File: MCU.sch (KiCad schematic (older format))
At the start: 42 parts, among them P801 JTAG, P802 A7, P803 M4, U801 MCIMX7D7DVM10SC, Y801 32kHz, Y802 24MHz

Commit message: This branch moves from i.mx7 to STM32F4 CPU to be finished for Hackaday Prize 2017
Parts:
- removed C805, C807, C810: 220n, Capacitors_SMD:C_0402, symbol C
- removed C806: 22u, Capacitors_SMD:C_0603, symbol C
- removed C808, C814, C815, C818: 2u2, Capacitors_SMD:C_0603, symbol C
- removed C809: 100n, Capacitors_SMD:C_0402, symbol C
- removed C811, C812, C813, C816, C817: 470n, Capacitors_SMD:C_0402, symbol C
- removed D801: D_Schottky, Diodes_SMD:DD-PAK_TO263_SingleDiode, symbol D_Schottky
- removed L801: 100R, Choke_SMD:Choke_SMD_1206_Standard, symbol L_Small
- removed P802: A7, Pin_Headers:Pin_Header_Straight_1x02, symbol CONN_01X02
- removed P803: M4, Pin_Headers:Pin_Header_Straight_1x02, symbol CONN_01X02
- removed R802, R810, R814, R815: 0, Resistors_SMD:R_0402, symbol R
- removed R803: 100k, Resistors_SMD:R_0402, symbol R
- removed R808: 10k, Resistors_SMD:R_0402, symbol R
- removed R809: 4k7, Resistors_SMD:R_0402, symbol R
- removed R811, R812: 1k, Resistors_SMD:R_0402, symbol R
- removed R813: 47k, Resistors_SMD:R_0402, symbol R
- removed U801: MCIMX7D7DVM10SC, NokiaRetroFit:BGA_541_075_19x19, symbol MCIMX7D7DVM10SC
- added C? (x8): 100n, Capacitors_SMD:C_0402, symbol C
- added C? (x2): 2u2, Capacitors_SMD:C_0402, symbol C
- added C?: 1u, Capacitors_SMD:C_0402, symbol C
- added J?: TEST_2P, symbol TEST_2P
- added R? (x2): 10k, symbol R
- added U?: STM32F756VGTx, LQFP100, symbol STM32F756VGTx
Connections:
- net labels added: ADC1, ADC2, ADC3, ADC_IN1, ADC_IN2, ADC_IN3, ETC_ALARM, I2C3_SCL, I2C3_SDA, I2C4_SCL, I2C4_SDA, JTAG_RST, JTAG_TCK, JTAG_TDI, JTAG_TDO, JTAG_TMS, LCD_RS, QSPI_BK2_IO0, QSPI_BK2_IO1, QSPI_BK2_IO2, QSPI_BK2_IO3, QSPI_BK2_NCS, QSPI_CLK, QSPI_IO0, QSPI_IO1, QSPI_IO2, QSPI_IO3, QSPI_NCS, RTC_OUT_ALARM, RTC_TS, SAI1_FS, SAI1_FS_A, SAI1_SCK, SAI1_SD, SAI1_SD_A, SAI_MCLK, SAI_MCLK_A, SDMMC1_CK, SDMMC1_CMD, SDMMC1_D0, SD_CK, SD_CMD, SD_D0, SYS_JRST, SYS_JTCK-SWCLK, SYS_JTDI, SYS_JTDO-SWO, SYS_JTMS-SWDIO, SYS_WKUP, TIM10_PWM, UART8_CTS, UART8_RTS, UART8_RX, UART8_TX, USART1_RX, USART1_TX, USART2_RX, USART2_TX, USART3_RX, USART3_TX, USART6_RX, USART6_TX, USB_DM, USB_DP, USB_ID, USB_OTG_HS_DM, USB_OTG_HS_DP, USB_OTG_HS_ID, USB_OTG_HS_VBUS, USB_VBUS, VBAT, nRST
- net labels removed: AT_UART0, AT_UART1, AT_UART2, AT_UART3, AT_UART[0..3], AT_UART_CTS, AT_UART_RTS, AT_UART_RX, AT_UART_TX, BT0, BT1, BT2, BT3, BT[0..7], BT_EN, BT_UART_CTS, BT_UART_RTS, BT_UART_RX, BT_UART_TX, D+, D-, GPIO2_D10, GPIO2_D11, GPIO2_D20, GPIO2_D21, GPIO2_D22, GPIO2_D23, GPIO2_D8, GPIO2_D9, GPS_TX, HST_DL0, HST_DL1, HST_DL[0..1], LCD_CLK, LCD_DATA00, LCD_DATA01, LCD_DATA02, LCD_DATA03, LCD_DATA04, LCD_DATA05, LCD_DATA06, LCD_DATA07, LCD_DATA08, LCD_DATA09, LCD_DATA10, LCD_DATA11, LCD_DATA12, LCD_DATA13, LCD_DATA14, LCD_DATA15, LCD_DATA16, LCD_DATA17, LCD_DATA18, LCD_DATA19, LCD_DATA20, LCD_DATA21, LCD_DATA22, LCD_DATA23, LCD_DATA[0..23], LCD_ENABLE, LCD_HSYNC, LCD_VSYNC, LED_PWM, NVCC_1V8, NVCC_3V3, PMIC_SD_VSEL, PWM1_OUT, PWM2_OUT, PWM3_OUT, PWM4_OUT, RADIO_ON, RUMBLE_EN, RUMBLE_PWM, SAI1[0..6], SAI2[0..3], SD2_BUS[0..8], SW2OUT, UART5_RX, UART7_CTS, UART7_RTS, UART7_RX, UART7_TX, USB_OTG_ID, VBAT_ref, VDC_ref, VDDA, VLDO4_2V8, VSNVS, V_USB_BUS_ref, ~ON, ~POR
- wire segments 223 -> 136
- no-connect marks 16 -> 1
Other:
- note removed: "10"
- note removed: "11"
- note removed: "12"
- note removed: "13"
- note removed: "1GB DDR3 RAM"
- note removed: "uSD-Card Slot\n8GB eMMC"
- moved on the sheet: C801, C802, C803, C804, P801, R801, R804, R805, R806, R807, TP801, Y801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

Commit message: Modification for STM32 adaption
For the Hackaday Prize 2017 I decided to switch to STM32 as CPU

*Power system was modified to just contain the charge IC,
*Boost converter for high voltage peripherals
*Buck converter for 3V3 for CPU and switchable NVCC_3V3
   for peripherie

CPU signals are routed and pinmux is done in firmware folder.

SD-Card has 4bit Interface

WiFi module ESP8266 is connected via UART

Wolfson Ausio codec is connected via SAI

Two digital microphones for noise canceling

Rumble Motor driver

LCD is connected via it's own I2C interface
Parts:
- C801, C802, C803, C804: footprint Capacitors_SMD:C_0402 -> Capacitors_SMD:C_0402_NoSilk
- C805, C806, C807, C808, C809, C810, C811, C812, C813, C814, C815: renamed from C?; footprint Capacitors_SMD:C_0402 -> Capacitors_SMD:C_0402_NoSilk
- J801: renamed from J?; footprint (none) -> Wire_Pads:SolderWirePad_2x_1mmDrill
- R801, R804, R805, R806, R807: footprint Resistors_SMD:R_0402 -> Resistors_SMD:R_0402_NoSilk
- R802, R803: renamed from R?; footprint (none) -> Resistors_SMD:R_0402_NoSilk
- gave numbers to parts that had none: 1
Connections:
- net I2C3_SCL: no longer U801.67 (I2C3_SCL/LTDC_R6/RCC_MCO_1/TIM1_CH1/TIM8_BKIN2/USART1_CK/USB_OTG_FS_SOF/PA8)
- net I2C3_SDA: no longer U801.66 (DAC_EXTI9/DCMI_D3/I2C3_SDA/I2S_CKIN/QUADSPI_BK1_IO0/RCC_MCO_2/SDMMC1_D1/TIM3_CH4/TIM8_CH4/UART5_CTS/PC9)
- net IMU_DRDY_M: now also U801.81 (PD0/CAN1_RX/FMC_D2/FMC_DA2); no longer U801.96 (CAN1_TX/DAC_EXTI9/DCMI_D7/I2C1_SDA/I2S2_WS/LTDC_B7/SDMMC1_D5/SPI2_NSS/TIM11_CH1/TIM4_CH4/PB9)
- net RADIO_ACTIVE: no longer U801.34 (ADC1_IN8/ADC2_IN8/ETH_RXD2/LTDC_R3/TIM1_CH2N/TIM3_CH3/TIM8_CH2N/UART4_CTS/USB_OTG_HS_ULPI_D1/PB0)
- net NVCC_3V3: now reaches C809.1, C810.1, C811.1, C812.1, C813.1, C814.1, C815.1, R803.2, U801.100 (VDD), U801.11 (VDD), U801.21 (VDDA), U801.27 (VDD), U801.50 (VDD), U801.75 (VDD)
- net WIFI_BOOT0: now reaches U801.15 (ADC1_IN10/ADC2_IN10/ADC3_IN10/FMC_SDNWE/LTDC_R5/SAI2_FS_B/USB_OTG_HS_ULPI_STP/PC0)
- net RADIO_ON: now reaches U801.17 (ADC1_IN12/ADC2_IN12/ADC3_IN12/ETH_TXD2/FMC_SDNE0/SPI2_MISO/USB_OTG_HS_ULPI_DIR/PC2)
- net SAI1_SDB: now reaches U801.2 (PE3/FMC_A19/SAI1_SD_B/SYS_TRACED0)
- net U3V3_PG: now reaches U801.32 (ADC1_IN14/ADC2_IN14/ETH_RXD0/FMC_SDNE0/I2S1_MCK/SPDIFRX_IN2/PC4)
- net WIFI_RESET: now reaches U801.70 (ADC1_EXTI11/ADC2_EXTI11/ADC3_EXTI11/CAN1_RX/LTDC_R4/TIM1_CH4/USART1_CTS/USB_OTG_FS_DM/PA11)
- net WIFI_CHPD: now reaches U801.71 (CAN1_TX/LTDC_R5/SAI2_FS_B/TIM1_ETR/USART1_RTS/USB_OTG_FS_DP/PA12)
- net SD_D2: now reaches U801.78 (DCMI_D8/I2S3_CK/LTDC_R2/QUADSPI_BK1_IO1/SDMMC1_D2/SPI3_SCK/UART4_TX/USART3_TX/PC10)
- net RUMBLE_EN: now reaches U801.82 (PD1/CAN1_TX/FMC_D3/FMC_DA3)
- net QSPI_CLK: no longer names the net of U801.36 (I2S3_SD/QUADSPI_CLK/SAI1_SD_A/SPI3_MOSI/PB2)
- net QSPI_CLK: no longer U801.37 (PE7/FMC_D4/FMC_DA4/QUADSPI_BK2_IO0/TIM1_ETR/UART7_RX)
- net QSPI_IO0 renamed PE8
- net QSPI_IO1 renamed PE9
- net QSPI_IO2 renamed PE10
- net QSPI_IO3 renamed NVCC_3V3_EN
- net QSPI_NCS renamed SD_D3
- net SAI1_SCK renamed SAI1_SCKA
- net SAI1_SD renamed SAI1_SDA
- new net AUDIO_INT: U801.34 (ADC1_IN8/ADC2_IN8/ETH_RXD2/LTDC_R3/TIM1_CH2N/TIM3_CH3/TIM8_CH2N/UART4_CTS/USB_OTG_HS_ULPI_D1/PB0)
- new net PE7: U801.37 (PE7/FMC_D4/FMC_DA4/QUADSPI_BK2_IO0/TIM1_ETR/UART7_RX)
- new net SD_D1: U801.66 (DAC_EXTI9/DCMI_D3/I2C3_SDA/I2S_CKIN/QUADSPI_BK1_IO0/RCC_MCO_2/SDMMC1_D1/TIM3_CH4/TIM8_CH4/UART5_CTS/PC9)
- new net TIM11_RUMBLE_PWM: U801.96 (CAN1_TX/DAC_EXTI9/DCMI_D7/I2C1_SDA/I2S2_WS/LTDC_B7/SDMMC1_D5/SPI2_NSS/TIM11_CH1/TIM4_CH4/PB9)

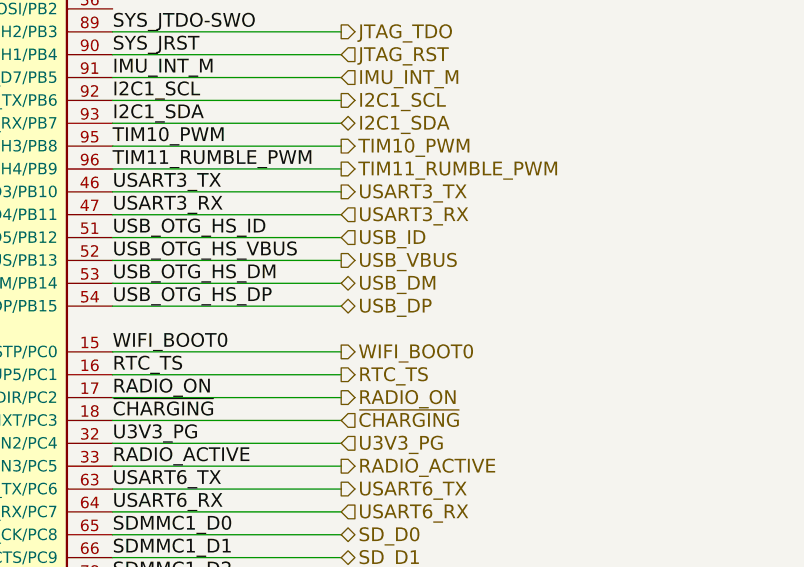
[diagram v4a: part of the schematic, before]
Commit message: Placed a lot of components and routed the audio codec
The BGA of tha audio chipset is to small for regualr technology.
We do not use all of the pins of the chip so we ignore the other
pads and escape throug the balls of the other pad.
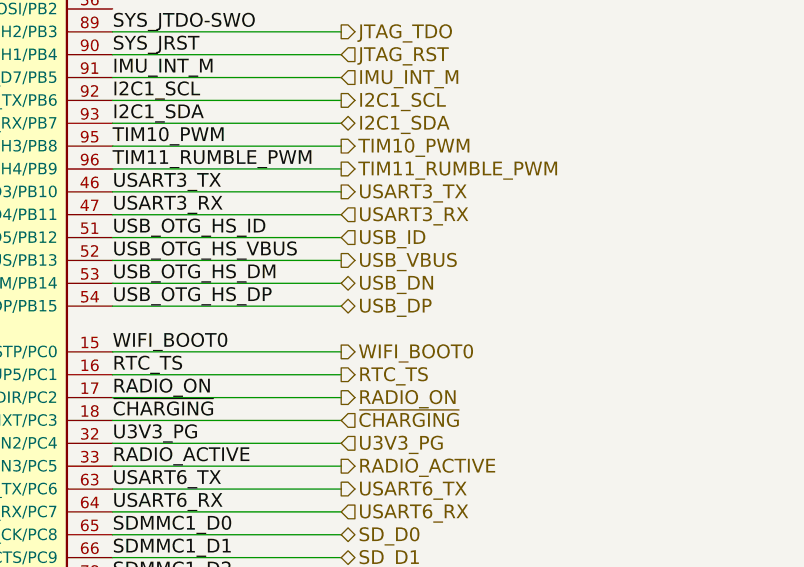
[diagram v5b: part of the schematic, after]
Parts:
- U801: footprint LQFP100 -> Housings_QFP:TQFP-100-1EP_14x14mm_Pitch0.5mm
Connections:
- net USB_DM renamed USB_DN
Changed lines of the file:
@@
 LIBS:contrib
 LIBS:valves
-LIBS:tps62742
-LIBS:WM8994ECS
+LIBS:stm32
 LIBS:3210retro-cache
 EELAYER 26 0
@@
 F 0 "U801" H 12850 8350 50  0000 C CNN
 F 1 "STM32F756VGTx" H 12650 2750 50  0000 C CNN
-F 2 "LQFP100" H 12950 8275 50  0001 R TNN
+F 2 "Housings_QFP:TQFP-100-1EP_14x14mm_Pitch0.5mm" H 12950 8275 50  0001 R TNN
 F 3 "" H 8050 5500 50  0001 C CNN
 	1    8050 5500
@@
 USB_VBUS
 Text HLabel 14150 6100 2    60   BiDi ~ 0
-USB_DM
+USB_DN
 Text HLabel 14150 6200 2    60   BiDi ~ 0
 USB_DP

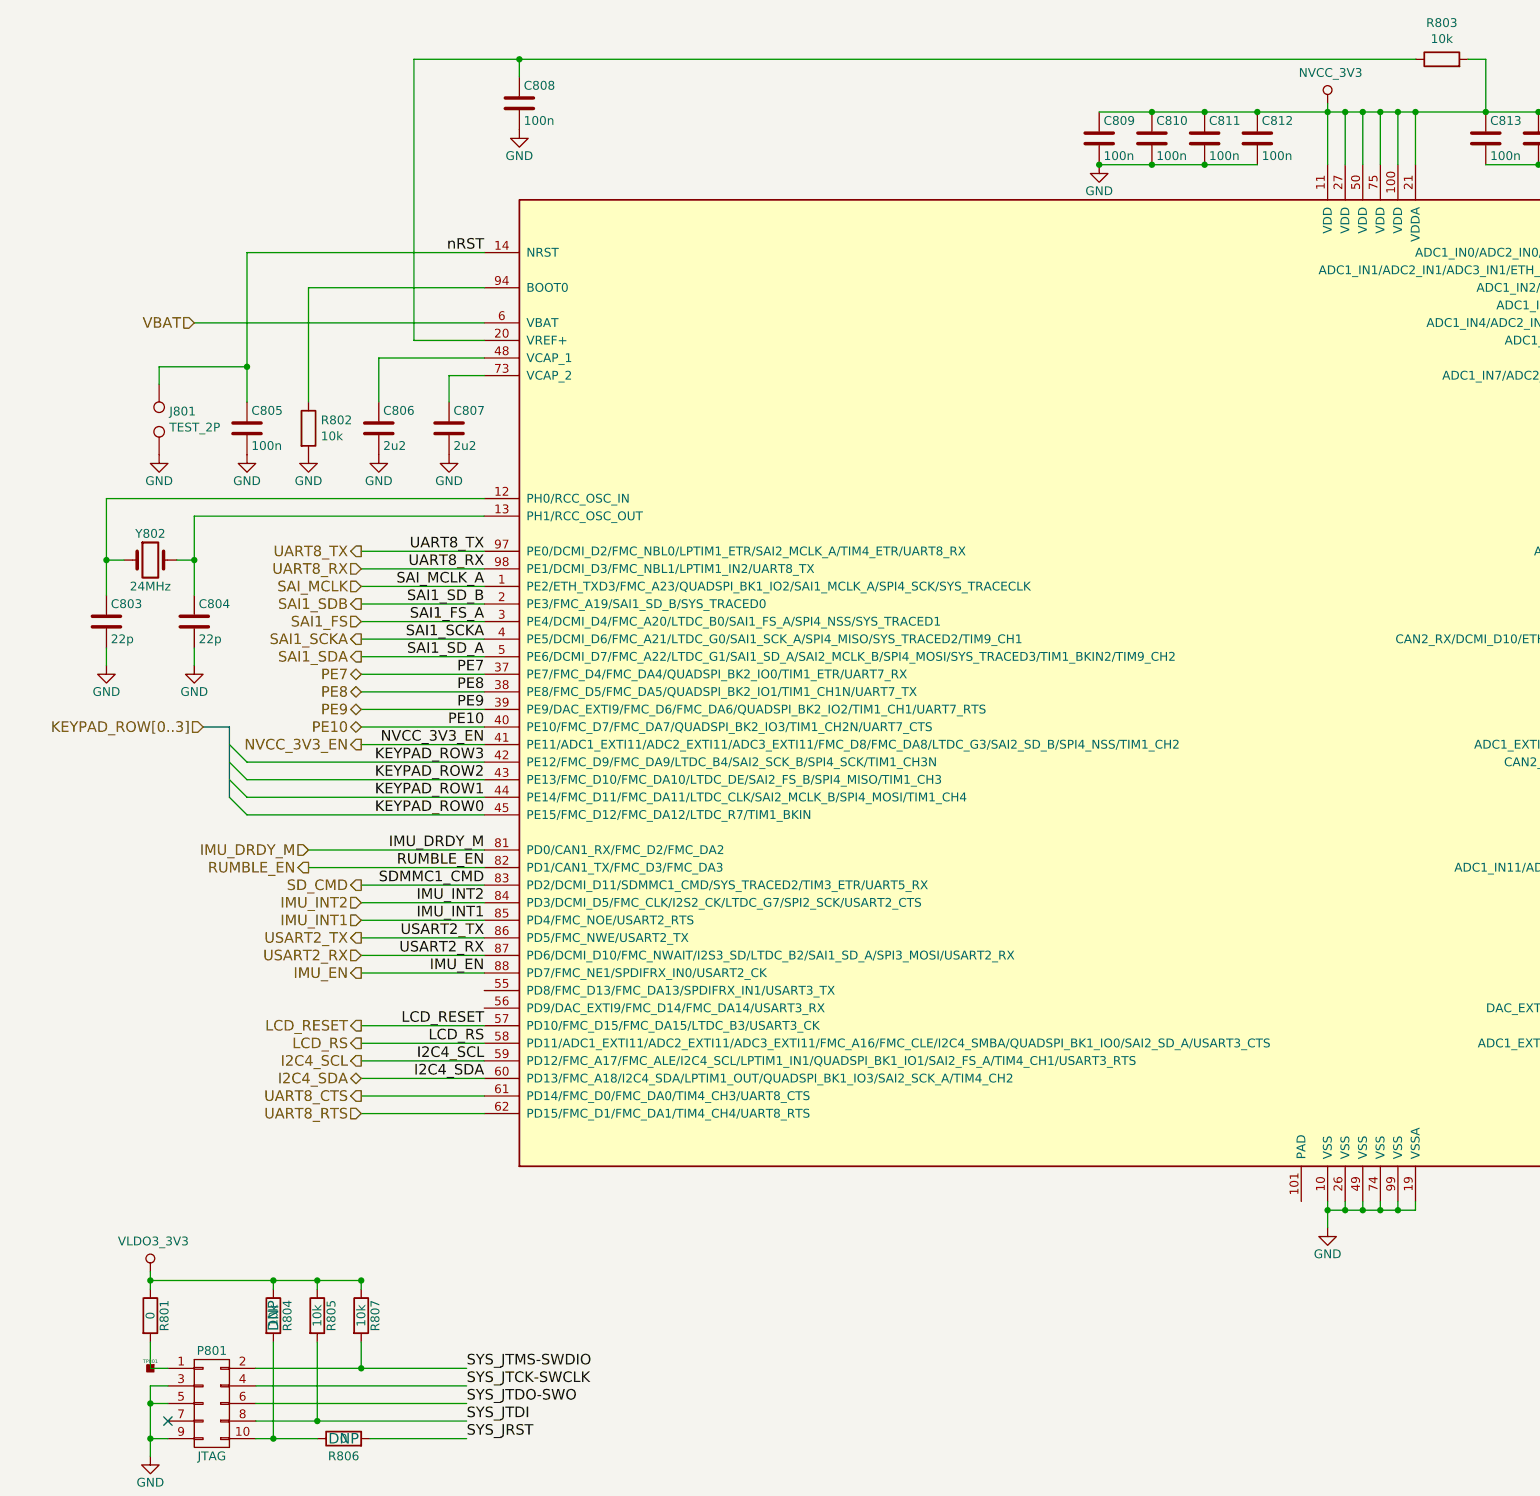
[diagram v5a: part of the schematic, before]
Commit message: Revision 1 of Layout
6layer board
through-hole via only (0.5/0.3mm drill)
0.2mm track width

https://hackaday.io/project/21263-nokia-3210-retro-fit-board/log/66914-prototype-pcb-done-there-comes-the-review
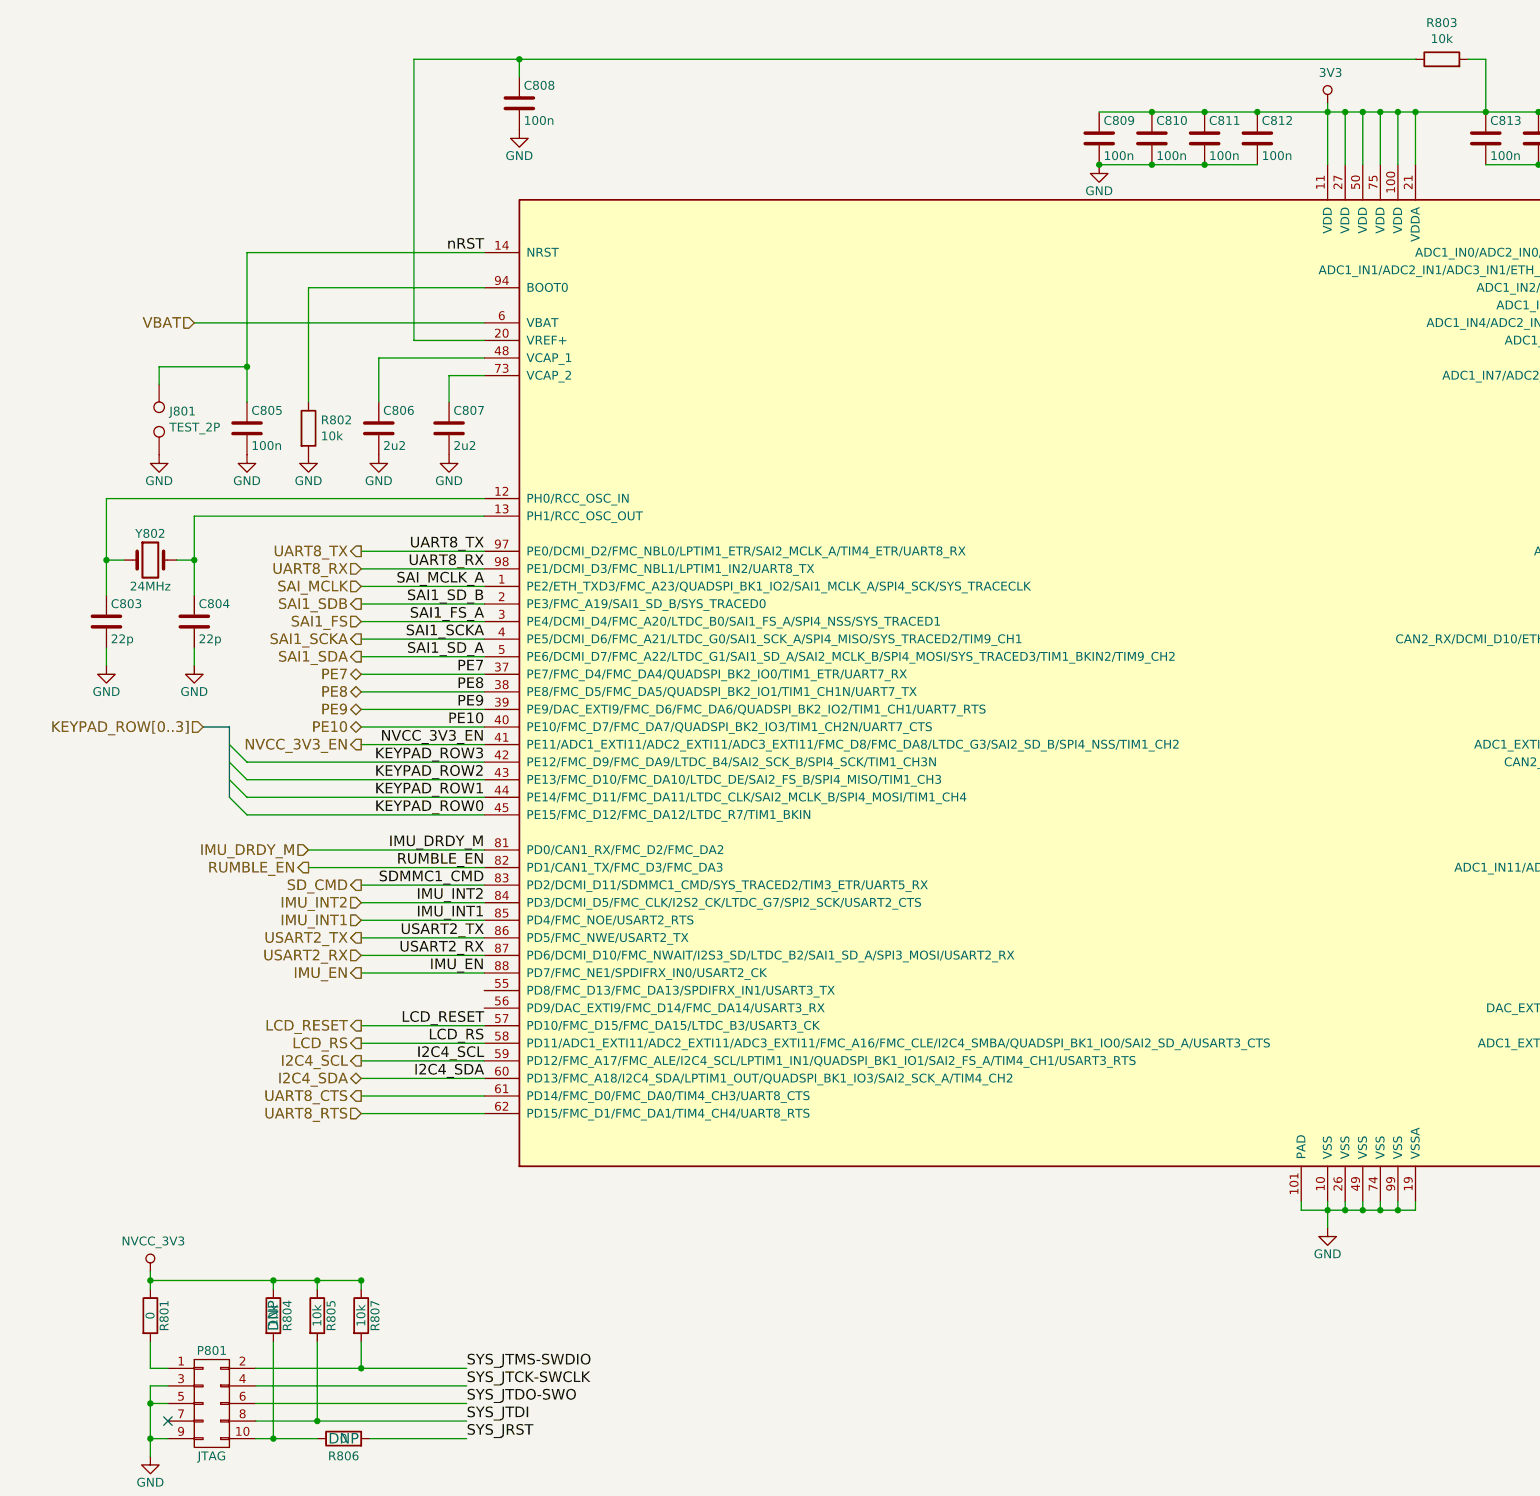
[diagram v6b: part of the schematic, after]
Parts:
- removed TP801: TP, NokiaRetroFit:TP, symbol TP
- J801: footprint Wire_Pads:SolderWirePad_2x_1mmDrill -> NokiaRetroFit:SolderWirePad_2x_0,8
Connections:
- net VLDO3_3V3 is gone; now on net NVCC_3V3: R801.1, R804.1, R805.1, R807.1
- net GND: now also U801.101 (PAD)
- net NVCC_3V3: no longer C809.1, C810.1, C811.1, C812.1, C813.1, C814.1, C815.1, R803.2, U801.100 (VDD), U801.11 (VDD), U801.21 (VDDA), U801.27 (VDD), U801.50 (VDD), U801.75 (VDD)
- new net 3V3: C809.1, C810.1, C811.1, C812.1, C813.1, C814.1, C815.1, R803.2, U801.100 (VDD), U801.11 (VDD), U801.21 (VDDA), U801.27 (VDD), U801.50 (VDD), U801.75 (VDD)
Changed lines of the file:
@@
 Date "2017-09-07"
 Rev "3"
-Comp "www.kurzschluss-blog.de"
+Comp "OSHW"
 Comment1 "Retro fitting board for Nokia 3210 mobile phone"
 Comment2 "STM32 Version"
@@
 	1    1050 9850
 	1    0    0    -1
-$EndComp
-$Comp
-L TP TP801
-U 1 1 585C5E44
-P 1050 9350
-F 0 "TP801" H 1050 9390 20  0000 C CNN
-F 1 "TP" H 1050 9300 60  0001 C CNN
-F 2 "NokiaRetroFit:TP" H 1050 9350 60  0001 C CNN
-F 3 "" H 1050 9350 60  0000 C CNN
-	1    1050 9350
-	-1   0    0    -1
 $EndComp
 Wire Bus Line
@@
 	2000 9200 2000 9650
 Connection ~ 2000 9650
-$Comp
-L VLDO3_3V3 #PWR0143
-U 1 1 593F88AF
-P 1050 8800
-F 0 "#PWR0143" H -1400 1700 50  0001 C CNN
-F 1 "VLDO3_3V3" H 1067 8973 50  0000 C CNN
-F 2 "" H -1400 1850 50  0001 C CNN
-F 3 "" H -1400 1850 50  0001 C CNN
-	1    1050 8800
-	1    0    0    -1
-$EndComp
 Wire Wire Line
 	1750 8850 1750 8900
@@
 	7750 8400 7750 8550
 Wire Wire Line
-	7750 8450 8250 8450
+	7600 8450 8250 8450
 Wire Wire Line
 	7850 8450 7850 8400
@@
 F 0 "J801" V 1054 3892 50  0000 R CNN
 F 1 "TEST_2P" V 1145 3892 50  0000 R CNN
-F 2 "Wire_Pads:SolderWirePad_2x_1mmDrill" H 1100 3950 50  0001 C CNN
+F 2 "NokiaRetroFit:SolderWirePad_2x_0,8" H 1100 3950 50  0001 C CNN
 F 3 "" H 1100 3950 50  0001 C CNN
 	1    1100 3950
@@
 Wire Wire Line
 	13150 6600 14150 6600
-$Comp
-L NVCC_3V3 #PWR0808
-U 1 1 59B49FE4
-P 7750 2150
-F 0 "#PWR0808" H 7750 2000 50  0001 C CNN
-F 1 "NVCC_3V3" H 7767 2323 50  0000 C CNN
-F 2 "" H 7750 2150 50  0001 C CNN
-F 3 "" H 7750 2150 50  0001 C CNN
-	1    7750 2150
-	1    0    0    -1
-$EndComp
 Text Label 2950 5800 2    60   ~ 0
 NVCC_3V3_EN
@@
 Wire Wire Line
 	2250 5700 2950 5700
+$Comp
+L 3V3 #PWR017
+U 1 1 59B5443C
+P 7750 2150
+F 0 "#PWR017" H 7750 2000 50  0001 C CNN
+F 1 "3V3" H 7767 2323 50  0000 C CNN
+F 2 "" H 7750 2150 50  0001 C CNN
+F 3 "" H 7750 2150 50  0001 C CNN
+	1    7750 2150
+	1    0    0    -1
+$EndComp
+Wire Wire Line
+	7600 8450 7600 8400
+$Comp
+L NVCC_3V3 #PWR019
+U 1 1 59B56807
+P 1050 8800
+F 0 "#PWR019" H 1050 8650 50  0001 C CNN
+F 1 "NVCC_3V3" H 1067 8973 50  0000 C CNN
+F 2 "" H 1050 8800 50  0001 C CNN
+F 3 "" H 1050 8800 50  0001 C CNN
+	1    1050 8800
+	1    0    0    -1
+$EndComp
 $EndSCHEMATC
